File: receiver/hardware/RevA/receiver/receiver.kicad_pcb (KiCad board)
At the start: 2 copper layers, 1 part, among them U1 C8051F850-A-GU

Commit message: ftdi and usb
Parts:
- added J1: 48037-0001, receiver:48037-0001, F.Cu at (33.8, 144.0)
- added U2: FT232RL, receiver:FT232RL, F.Cu at (38.4, 141.0)
- moved U1 5.24 mm to (49.5, 142.2)
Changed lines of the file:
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@@
     (tracks 0)
     (zones 0)
-    (modules 1)
-    (nets 25)
+    (modules 3)
+    (nets 59)
   )
   (page A4)
@@
     (31 B.Cu signal)
     (32 B.Adhes user)
-    (33 F.Adhes user)
+    (33 F.Adhes user hide)
     (34 B.Paste user)
     (35 F.Paste user)
     (36 B.SilkS user)
     (37 F.SilkS user)
-    (38 B.Mask user)
-    (39 F.Mask user)
+    (38 B.Mask user hide)
+    (39 F.Mask user hide)
     (40 Dwgs.User user)
     (41 Cmts.User user)
     (42 Eco1.User user)
-    (43 Eco2.User user)
-    (44 Edge.Cuts user)
+    (43 Eco2.User user hide)
+    (44 Edge.Cuts user hide)
     (45 Margin user)
     (46 B.CrtYd user)
@@
   (net 23 "Net-(U1-Pad2)")
   (net 24 "Net-(U1-Pad1)")
+  (net 25 "Net-(U2-Pad28)")
+  (net 26 "Net-(U2-Pad27)")
+  (net 27 "Net-(U2-Pad26)")
+  (net 28 "Net-(U2-Pad25)")
+  (net 29 "Net-(U2-Pad24)")
+  (net 30 "Net-(U2-Pad23)")
+  (net 31 "Net-(U2-Pad22)")
+  (net 32 "Net-(U2-Pad21)")
+  (net 33 "Net-(U2-Pad20)")
+  (net 34 "Net-(U2-Pad19)")
+  (net 35 "Net-(U2-Pad18)")
+  (net 36 "Net-(U2-Pad17)")
+  (net 37 "Net-(U2-Pad16)")
+  (net 38 "Net-(U2-Pad15)")
+  (net 39 "Net-(U2-Pad14)")
+  (net 40 "Net-(U2-Pad13)")
+  (net 41 "Net-(U2-Pad12)")
+  (net 42 "Net-(U2-Pad11)")
+  (net 43 "Net-(U2-Pad10)")
+  (net 44 "Net-(U2-Pad9)")
+  (net 45 "Net-(U2-Pad8)")
+  (net 46 "Net-(U2-Pad7)")
+  (net 47 "Net-(U2-Pad6)")
+  (net 48 "Net-(U2-Pad5)")
+  (net 49 "Net-(U2-Pad4)")
+  (net 50 "Net-(U2-Pad3)")
+  (net 51 "Net-(U2-Pad2)")
+  (net 52 "Net-(U2-Pad1)")
+  (net 53 "Net-(J1-Pad6)")
+  (net 54 "Net-(J1-Pad5)")
+  (net 55 "Net-(J1-Pad4)")
+  (net 56 "Net-(J1-Pad3)")
+  (net 57 "Net-(J1-Pad2)")
+  (net 58 "Net-(J1-Pad1)")
   (net_class Default "This is the default net class."
     (clearance 0.2)
@@
     (uvia_dia 0.3)
     (uvia_drill 0.1)
+    (add_net "Net-(J1-Pad1)")
+    (add_net "Net-(J1-Pad2)")
+    (add_net "Net-(J1-Pad3)")
+    (add_net "Net-(J1-Pad4)")
+    (add_net "Net-(J1-Pad5)")
+    (add_net "Net-(J1-Pad6)")
     (add_net "Net-(U1-Pad1)")
     (add_net "Net-(U1-Pad10)")
@@
     (add_net "Net-(U1-Pad8)")
     (add_net "Net-(U1-Pad9)")
+    (add_net "Net-(U2-Pad1)")
+    (add_net "Net-(U2-Pad10)")
+    (add_net "Net-(U2-Pad11)")
+    (add_net "Net-(U2-Pad12)")
+    (add_net "Net-(U2-Pad13)")
+    (add_net "Net-(U2-Pad14)")
+    (add_net "Net-(U2-Pad15)")
+    (add_net "Net-(U2-Pad16)")
+    (add_net "Net-(U2-Pad17)")
+    (add_net "Net-(U2-Pad18)")
+    (add_net "Net-(U2-Pad19)")
+    (add_net "Net-(U2-Pad2)")
+    (add_net "Net-(U2-Pad20)")
+    (add_net "Net-(U2-Pad21)")
+    (add_net "Net-(U2-Pad22)")
+    (add_net "Net-(U2-Pad23)")
+    (add_net "Net-(U2-Pad24)")
+    (add_net "Net-(U2-Pad25)")
+    (add_net "Net-(U2-Pad26)")
+    (add_net "Net-(U2-Pad27)")
+    (add_net "Net-(U2-Pad28)")
+    (add_net "Net-(U2-Pad3)")
+    (add_net "Net-(U2-Pad4)")
+    (add_net "Net-(U2-Pad5)")
+    (add_net "Net-(U2-Pad6)")
+    (add_net "Net-(U2-Pad7)")
+    (add_net "Net-(U2-Pad8)")
+    (add_net "Net-(U2-Pad9)")
+  )
+  (module receiver:48037-0001 (layer F.Cu)
+    (at 33.782 144.018 270)
+    (fp_text reference J1 (at 9.1 2.1 90) (layer F.SilkS)
+      (effects (font (size 1 1) (thickness 0.15)))
+    )
+    (fp_text value 48037-0001 (at -13.97 1.778 90) (layer F.Fab)
+      (effects (font (size 1 1) (thickness 0.15)))
+    )
+    (fp_line (start -6 -1) (end -6 -0.1) (layer F.SilkS) (width 0.12))
+    (fp_line (start 6 -1) (end -6 -1) (layer F.SilkS) (width 0.12))
+    (fp_line (start 6 -0.1) (end 6 -1) (layer F.SilkS) (width 0.12))
+    (fp_line (start 6 4.85) (end 6 4.3) (layer F.SilkS) (width 0.12))
+    (fp_line (start -6 4.85) (end -6 4.3) (layer F.SilkS) (width 0.12))
+    (fp_line (start -6 4.85) (end 6 4.85) (layer F.SilkS) (width 0.12))
+    (pad "" np_thru_hole circle (at 2.25 2.1) (size 1.1 1.1) (drill 1.1) (layers *.Cu *.Mask))
+    (pad "" np_thru_hole circle (at -2.25 2.1) (size 1.1 1.1) (drill 1.1) (layers *.Cu *.Mask))
+    (pad 6 thru_hole oval (at 5.7 2.1 90) (size 2 4.2) (drill oval 1 2.5) (layers *.Cu *.Mask)
+      (net 53 "Net-(J1-Pad6)"))
+    (pad 5 thru_hole oval (at -5.7 2.1 90) (size 2 4.2) (drill oval 1 2.5) (layers *.Cu *.Mask)
+      (net 54 "Net-(J1-Pad5)"))
+    (pad 4 thru_hole circle (at -3.5 0 270) (size 1.5 1.5) (drill 0.92) (layers *.Cu *.Mask)
+      (net 55 "Net-(J1-Pad4)"))
+    (pad 3 thru_hole circle (at -1 0 270) (size 1.5 1.5) (drill 0.92) (layers *.Cu *.Mask)
+      (net 56 "Net-(J1-Pad3)"))
+    (pad 2 thru_hole circle (at 1 0 270) (size 1.5 1.5) (drill 0.92) (layers *.Cu *.Mask)
+      (net 57 "Net-(J1-Pad2)"))
+    (pad 1 thru_hole circle (at 3.5 0 270) (size 1.5 1.5) (drill 0.92) (layers *.Cu *.Mask)
+      (net 58 "Net-(J1-Pad1)"))
+  )
+  (module receiver:FT232RL (layer F.Cu)
+    (at 38.354 140.97)
+    (fp_text reference U2 (at 3 -1.8) (layer F.SilkS)
+      (effects (font (size 1 1) (thickness 0.15)))
+    )
+    (fp_text value FT232RL (at 1.6 -5.2) (layer F.Fab)
+      (effects (font (size 1 1) (thickness 0.15)))
+    )
+    (fp_circle (center 0.2 -1.1) (end 0.4 -1) (layer F.SilkS) (width 0.12))
+    (fp_line (start 5.7 -1) (end 1 -1) (layer F.SilkS) (width 0.12))
+    (fp_line (start 5.7 9.2) (end 5.7 -1) (layer F.SilkS) (width 0.12))
+    (fp_line (start 1 9.2) (end 5.7 9.2) (layer F.SilkS) (width 0.12))
+    (fp_line (start 1 -1) (end 1 9.2) (layer F.SilkS) (width 0.12))
+    (pad 28 smd roundrect (at 6.8 0) (size 1.5 0.4) (layers F.Cu F.Paste F.Mask) (roundrect_rratio 0.25)
+      (net 25 "Net-(U2-Pad28)"))
+    (pad 27 smd roundrect (at 6.8 0.65) (size 1.5 0.4) (layers F.Cu F.Paste F.Mask) (roundrect_rratio 0.25)
+      (net 26 "Net-(U2-Pad27)"))
+    (pad 26 smd roundrect (at 6.8 1.3) (size 1.5 0.4) (layers F.Cu F.Paste F.Mask) (roundrect_rratio 0.25)
+      (net 27 "Net-(U2-Pad26)"))
+    (pad 25 smd roundrect (at 6.8 1.95) (size 1.5 0.4) (layers F.Cu F.Paste F.Mask) (roundrect_rratio 0.25)
+      (net 28 "Net-(U2-Pad25)"))
+    (pad 24 smd roundrect (at 6.8 2.6) (size 1.5 0.4) (layers F.Cu F.Paste F.Mask) (roundrect_rratio 0.25)
+      (net 29 "Net-(U2-Pad24)"))
+    (pad 23 smd roundrect (at 6.8 3.25) (size 1.5 0.4) (layers F.Cu F.Paste F.Mask) (roundrect_rratio 0.25)
+      (net 30 "Net-(U2-Pad23)"))
+    (pad 22 smd roundrect (at 6.8 3.9) (size 1.5 0.4) (layers F.Cu F.Paste F.Mask) (roundrect_rratio 0.25)
+      (net 31 "Net-(U2-Pad22)"))
+    (pad 21 smd roundrect (at 6.8 4.55) (size 1.5 0.4) (layers F.Cu F.Paste F.Mask) (roundrect_rratio 0.25)
+      (net 32 "Net-(U2-Pad21)"))
+    (pad 20 smd roundrect (at 6.8 5.2) (size 1.5 0.4) (layers F.Cu F.Paste F.Mask) (roundrect_rratio 0.25)
+      (net 33 "Net-(U2-Pad20)"))
+    (pad 19 smd roundrect (at 6.8 5.85) (size 1.5 0.4) (layers F.Cu F.Paste F.Mask) (roundrect_rratio 0.25)
+      (net 34 "Net-(U2-Pad19)"))
+    (pad 18 smd roundrect (at 6.8 6.5) (size 1.5 0.4) (layers F.Cu F.Paste F.Mask) (roundrect_rratio 0.25)
+      (net 35 "Net-(U2-Pad18)"))
+    (pad 17 smd roundrect (at 6.8 7.15) (size 1.5 0.4) (layers F.Cu F.Paste F.Mask) (roundrect_rratio 0.25)
+      (net 36 "Net-(U2-Pad17)"))
+    (pad 16 smd roundrect (at 6.8 7.8) (size 1.5 0.4) (layers F.Cu F.Paste F.Mask) (roundrect_rratio 0.25)
+      (net 37 "Net-(U2-Pad16)"))
+    (pad 15 smd roundrect (at 6.8 8.45) (size 1.5 0.4) (layers F.Cu F.Paste F.Mask) (roundrect_rratio 0.25)
+      (net 38 "Net-(U2-Pad15)"))
+    (pad 14 smd roundrect (at 0 8.45) (size 1.5 0.4) (layers F.Cu F.Paste F.Mask) (roundrect_rratio 0.25)
+      (net 39 "Net-(U2-Pad14)"))
+    (pad 13 smd roundrect (at 0 7.8) (size 1.5 0.4) (layers F.Cu F.Paste F.Mask) (roundrect_rratio 0.25)
+      (net 40 "Net-(U2-Pad13)"))
+    (pad 12 smd roundrect (at 0 7.15) (size 1.5 0.4) (layers F.Cu F.Paste F.Mask) (roundrect_rratio 0.25)
+      (net 41 "Net-(U2-Pad12)"))
+    (pad 11 smd roundrect (at 0 6.5) (size 1.5 0.4) (layers F.Cu F.Paste F.Mask) (roundrect_rratio 0.25)
+      (net 42 "Net-(U2-Pad11)"))
+    (pad 10 smd roundrect (at 0 5.85) (size 1.5 0.4) (layers F.Cu F.Paste F.Mask) (roundrect_rratio 0.25)
+      (net 43 "Net-(U2-Pad10)"))
+    (pad 9 smd roundrect (at 0 5.2) (size 1.5 0.4) (layers F.Cu F.Paste F.Mask) (roundrect_rratio 0.25)
+      (net 44 "Net-(U2-Pad9)"))
+    (pad 8 smd roundrect (at 0 4.55) (size 1.5 0.4) (layers F.Cu F.Paste F.Mask) (roundrect_rratio 0.25)
+      (net 45 "Net-(U2-Pad8)"))
+    (pad 7 smd roundrect (at 0 3.9) (size 1.5 0.4) (layers F.Cu F.Paste F.Mask) (roundrect_rratio 0.25)
+      (net 46 "Net-(U2-Pad7)"))
+    (pad 6 smd roundrect (at 0 3.25) (size 1.5 0.4) (layers F.Cu F.Paste F.Mask) (roundrect_rratio 0.25)
+      (net 47 "Net-(U2-Pad6)"))
+    (pad 5 smd roundrect (at 0 2.6) (size 1.5 0.4) (layers F.Cu F.Paste F.Mask) (roundrect_rratio 0.25)
+      (net 48 "Net-(U2-Pad5)"))
+    (pad 4 smd roundrect (at 0 1.95) (size 1.5 0.4) (layers F.Cu F.Paste F.Mask) (roundrect_rratio 0.25)
+      (net 49 "Net-(U2-Pad4)"))
+    (pad 3 smd roundrect (at 0 1.3) (size 1.5 0.4) (layers F.Cu F.Paste F.Mask) (roundrect_rratio 0.25)
+      (net 50 "Net-(U2-Pad3)"))
+    (pad 2 smd roundrect (at 0 0.65) (size 1.5 0.4) (layers F.Cu F.Paste F.Mask) (roundrect_rratio 0.25)
+      (net 51 "Net-(U2-Pad2)"))
+    (pad 1 smd roundrect (at 0 0) (size 1.5 0.4) (layers F.Cu F.Paste F.Mask) (roundrect_rratio 0.25)
+      (net 52 "Net-(U2-Pad1)"))
   )
   (module receiver:C8051F850-A-GU (layer F.Cu)
-    (at 44.45 143.51)
+    (at 49.53 142.24)
     (fp_text reference U1 (at 3 -1.64) (layer F.SilkS)
       (effects (font (size 1 1) (thickness 0.15)))

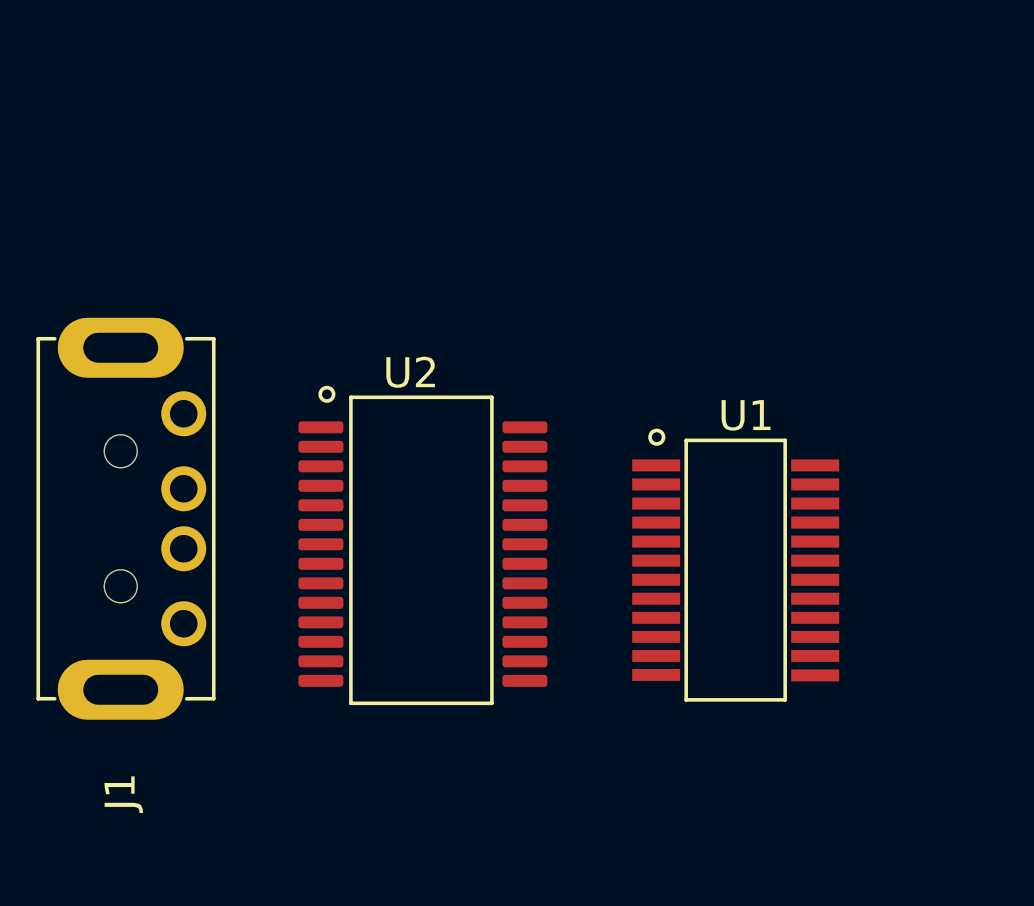
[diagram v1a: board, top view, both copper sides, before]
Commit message: add connector
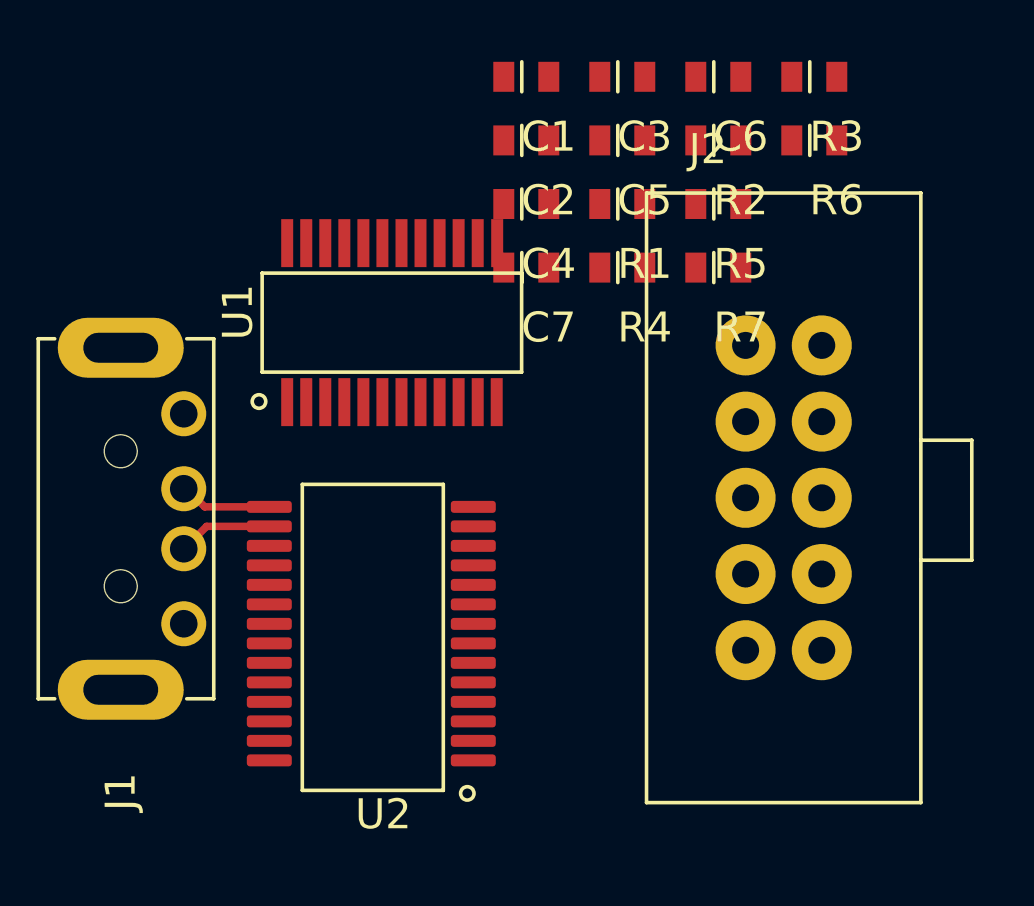
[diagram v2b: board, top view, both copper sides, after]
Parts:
- added C1: CAP_0603, receiver:0603, F.Cu at (44.5, 129.3)
- added C2: CAP_0603, receiver:0603, F.Cu at (44.5, 131.4)
- added C3: CAP_0603, receiver:0603, F.Cu at (47.6, 129.3)
- added C4: CAP_0603, receiver:0603, F.Cu at (44.5, 133.5)
- added C5: CAP_0603, receiver:0603, F.Cu at (47.6, 131.4)
- added C6: CAP_0603, receiver:0603, F.Cu at (50.9, 129.3)
- added C7: CAP_0603, receiver:0603, F.Cu at (44.5, 135.6)
- added J2: 5103309-1, receiver:5103309-1, F.Cu at (55.0, 148.4)
- added R1: RES_0603, receiver:0603, F.Cu at (47.6, 133.5)
- added R2: RES_0603, receiver:0603, F.Cu at (50.9, 131.4)
- added R3: RES_0603, receiver:0603, F.Cu at (54.0, 129.3)
- added R4: RES_0603, receiver:0603, F.Cu at (47.6, 135.6)
- added R5: RES_0603, receiver:0603, F.Cu at (50.9, 133.5)
- added R6: RES_0603, receiver:0603, F.Cu at (54.0, 131.4)
- added R7: RES_0603, receiver:0603, F.Cu at (50.9, 135.6)
- moved U1 12.5 mm to (37.2, 140.1), turned to 90 degrees
- moved U2 12.2 mm to (43.4, 152.1), turned to 180 degrees
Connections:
- net Net-(U2-Pad1) renamed /FT_TO_MCU
- net Net-(U2-Pad5) renamed /MCU_TO_FT
- J1 pad 1: Net-(J1-Pad1) -> +5V
- J1 pad 4: Net-(J1-Pad4) -> GND
- J1 pad 5: Net-(J1-Pad5) -> GND
- J1 pad 6: Net-(J1-Pad6) -> GND
- U1 pad 5: Net-(U1-Pad5) -> GND
- U1 pad 6: Net-(U1-Pad6) -> +3V3
- U2 pad 15: Net-(U2-Pad15) -> Net-(J1-Pad3)
- U2 pad 16: Net-(U2-Pad16) -> Net-(J1-Pad2)
- U2 pad 17: Net-(U2-Pad17) -> +3V3
- U2 pad 18: Net-(U2-Pad18) -> GND
- U2 pad 20: Net-(U2-Pad20) -> +5V
- U2 pad 21: Net-(U2-Pad21) -> GND
- U2 pad 25: Net-(U2-Pad25) -> GND
- U2 pad 26: Net-(U2-Pad26) -> GND
- U2 pad 4: Net-(U2-Pad4) -> +3V3
- U2 pad 7: Net-(U2-Pad7) -> GND
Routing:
- net Net-(J1-Pad2): track 0.00 -> 3.17 mm
- net Net-(J1-Pad3): track 0.00 -> 3.13 mm

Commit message: connectors
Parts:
- added J3: 2212S-04SG-85, receiver:2212S-04SG-85, F.Cu at (68.6, 139.4)
- added R10: RES_0603, receiver:0603, F.Cu at (70.9, 123.2)
- added R8: RES_0603, receiver:0603, F.Cu at (63.1, 134.9)
- added R9: RES_0603, receiver:0603, F.Cu at (67.7, 123.2)
- added T00: TestPoints, receiver:TestPoint, F.Cu at (74.7, 123.6)
- added T01: TestPoints, receiver:TestPoint, F.Cu at (68.3, 125.7)
- added T02: TestPoints, receiver:TestPoint, F.Cu at (71.3, 125.7)
- added T03: TestPoints, receiver:TestPoint, F.Cu at (68.3, 128.7)
- added T04: TestPoints, receiver:TestPoint, F.Cu at (71.3, 128.7)
- added T05: TestPoints, receiver:TestPoint, F.Cu at (68.3, 131.7)
- added T06: TestPoints, receiver:TestPoint, F.Cu at (66.9, 135.4)
- added T07: TestPoints, receiver:TestPoint, F.Cu at (77.7, 123.6)
- added T10: TestPoints, receiver:TestPoint, F.Cu at (74.3, 126.6)
- added T11: TestPoints, receiver:TestPoint, F.Cu at (71.3, 131.7)
- added T12: TestPoints, receiver:TestPoint, F.Cu at (77.3, 126.6)
- added T13: TestPoints, receiver:TestPoint, F.Cu at (74.3, 129.6)
- added T14: TestPoints, receiver:TestPoint, F.Cu at (80.7, 123.6)
- added T15: TestPoints, receiver:TestPoint, F.Cu at (69.9, 134.7)
- added T16: TestPoints, receiver:TestPoint, F.Cu at (77.3, 129.6)
- added T17: TestPoints, receiver:TestPoint, F.Cu at (80.3, 126.6)
- added T21: TestPoints, receiver:TestPoint, F.Cu at (74.3, 132.6)
- added T31: TestPoints, receiver:TestPoint, F.Cu at (83.7, 123.6)
- added T32: TestPoints, receiver:TestPoint, F.Cu at (77.3, 132.6)
- added T33: TestPoints, receiver:TestPoint, F.Cu at (80.3, 129.6)
- added T40: TestPoints, receiver:TestPoint, F.Cu at (83.3, 126.6)
- added T41: TestPoints, receiver:TestPoint, F.Cu at (72.9, 135.6)
- added T42: TestPoints, receiver:TestPoint, F.Cu at (86.7, 123.6)
- added T43: TestPoints, receiver:TestPoint, F.Cu at (75.9, 135.6)
- added T44: TestPoints, receiver:TestPoint, F.Cu at (80.3, 132.6)
- added T45: TestPoints, receiver:TestPoint, F.Cu at (83.3, 129.6)
- added T46: TestPoints, receiver:TestPoint, F.Cu at (86.3, 126.6)
- added T47: TestPoints, receiver:TestPoint, F.Cu at (78.9, 135.6)
- added T48: TestPoints, receiver:TestPoint, F.Cu at (83.3, 132.6)
- added T49: TestPoints, receiver:TestPoint, F.Cu at (86.1, 143.0)
- added T50: TestPoints, receiver:TestPoint, F.Cu at (81.9, 135.6)
- moved U1 8.42 mm to (45.6, 141.2)
- moved J2 1.02 mm to (55.1, 149.4), turned to 270 degrees
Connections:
- J2 pad 10: Net-(J2-Pad10) -> /USB_PWR
- J2 pad 2: Net-(J2-Pad2) -> GND
- J2 pad 3: Net-(J2-Pad3) -> GND
- J2 pad 4: Net-(J2-Pad4) -> /TCK_C2D
- J2 pad 5: Net-(J2-Pad5) -> /TMS_C2CK
- J2 pad 6: Net-(J2-Pad6) -> /TDO_C2D
- J2 pad 7: Net-(J2-Pad7) -> /TDI_C2CK
- J2 pad 9: Net-(J2-Pad9) -> GND
- U1 pad 19: Net-(U1-Pad19) -> /RX
- U1 pad 21: Net-(U1-Pad21) -> /FT_TO_MCU
- U1 pad 22: Net-(U1-Pad22) -> /MCU_TO_FT
- U1 pad 7: Net-(U1-Pad7) -> /TDI_C2CK
- U1 pad 8: Net-(U1-Pad8) -> /TCK_C2D

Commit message: edge cuts
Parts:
- added C8: CAP_0603, receiver:0603, F.Cu at (66.5, 172.7)
- C5, T00, T04, T05, T06, T07, T11, T12, T16, T17, T31, T32, T33, T44, T45, T46, T47, T49: moved to B.Cu
- moved T05 63.3 mm to (40.6, 188.6)
- moved T33 60.3 mm to (61.3, 186.8)
- moved T00 60.2 mm to (47.2, 177.2)
- moved C3 59.7 mm to (33.2, 187.2), turned to 270 degrees
- moved T48 59.2 mm to (37.4, 170.0)
- moved C1 58.7 mm to (35.3, 187.2), turned to 270 degrees
- moved T49 58.1 mm to (34.6, 169.9)
- moved T46 58.1 mm to (60.4, 178.6)
- moved T45 57.9 mm to (72.8, 186.6)
- moved T31 57.6 mm to (71.8, 179.9)
- moved T10 57.1 mm to (39.9, 172.2)
- moved R3 57.1 mm to (50.3, 186.3), turned to 270 degrees
- moved T44 57.1 mm to (69.5, 188.6)
- moved R10 56.6 mm to (52.8, 176.8)
- moved T04 55.8 mm to (37.5, 173.2)
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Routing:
- net GND: track 0.00 -> 98.4 mm, vias 0 -> 2
- net +3V3: track 0.00 -> 68.0 mm
- net /TDI_C2CK: track 0.00 -> 41.8 mm, vias 0 -> 1
- net /RX: track 0.00 -> 30.8 mm, vias 0 -> 1
- net /MCU_TO_FT: track 0.00 -> 25.4 mm, vias 0 -> 1
- net /FT_TO_MCU: track 0.00 -> 23.1 mm, vias 0 -> 1
- net /TCK_C2D: track 0.00 -> 20.8 mm, vias 0 -> 1
- net +5V: track 0.00 -> 20.6 mm, vias 0 -> 1
- net Net-(R2-Pad1): track 0.00 -> 10.1 mm, vias 0 -> 2
- net Net-(T06-Pad1): track 0.00 -> 10.0 mm, vias 0 -> 1
- net Net-(C8-Pad1): track 0.00 -> 9.77 mm
- net Net-(R7-Pad1): track 0.00 -> 8.58 mm
- net Net-(T13-Pad1): track 0.00 -> 8.03 mm
- net Net-(T16-Pad1): track 0.00 -> 7.18 mm, vias 0 -> 1
- net Net-(R4-Pad1): track 0.00 -> 6.66 mm
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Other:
- board outline added: 45 x 22 mm

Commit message: finish layout
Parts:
- C1, C3, T10, T40, T41, T43: moved to B.Cu
- T00, T16, T17, T33: moved to F.Cu
- moved T43 24.5 mm to (38.6, 169.3)
- moved T10 22.3 mm to (62.0, 169.4)
- moved T42 18.4 mm to (52.3, 183.2)
- moved T45 15.2 mm to (57.5, 186.7)
- moved T46 11.3 mm to (71.4, 181.1)
- moved T11 9.46 mm to (59.4, 169.4)
- moved T32 8.59 mm to (71.4, 183.6)
- moved T00 8.51 mm to (43.7, 169.4)
- moved C1 8.19 mm to (39.5, 180.2), turned to 0 degrees
- moved T17 7.42 mm to (62.0, 172.2)
- moved T06 7.11 mm to (54.4, 169.4)
- moved T04 7.07 mm to (44.3, 175.0)
- moved T16 6.86 mm to (62.0, 174.8)
- moved T05 6.29 mm to (46.1, 185.5)
- moved T31 6.25 mm to (71.4, 186.2)
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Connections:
- net Net-(C8-Pad1) renamed VCC
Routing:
- net +5V: track 20.6 -> 72.6 mm, vias 1 -> 8
- net /TDI_C2CK: track 41.8 -> 24.4 mm
- net Net-(R3-Pad1): track 0.00 -> 16.9 mm, vias 0 -> 2
- net Net-(T01-Pad1): track 0.00 -> 16.4 mm
- net Net-(T10-Pad1): track 0.00 -> 15.2 mm, vias 0 -> 1
- net Net-(T02-Pad1): track 0.00 -> 13.7 mm
- net GND: track 98.4 -> 112.0 mm, vias 2 -> 86
- net Net-(T00-Pad1): track 0.00 -> 11.5 mm
- net /TDO_C2D: track 3.47 -> 12.2 mm
- net Net-(R1-Pad2): track 0.00 -> 8.48 mm, vias 0 -> 2
- net /FT_TO_MCU: track 23.1 -> 29.9 mm, vias 1 -> 2
- net Net-(T11-Pad1): track 5.01 -> 11.1 mm
- net Net-(T17-Pad1): track 6.15 -> 11.6 mm, vias 1 -> 0
- net VCC: track 9.77 -> 5.04 mm
- net /TCK_C2D: track 20.8 -> 25.4 mm
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- added copper zone on F.Cu, net +3V3
- added copper zone on B.Cu, net +5V
- added copper zone on B.Cu, net GND
- added copper zone on F.Cu, net GND
- added copper zone on F.Cu, net VCC
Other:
- board text added: "AJR"
- board text added: "Dec 2021 Rev A"
